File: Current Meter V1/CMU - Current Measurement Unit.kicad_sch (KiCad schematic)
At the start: 0 parts

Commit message: Initial commit
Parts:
- added C114, C115, C116, C117, C119, C122, C123, C124: 100nF, symbol Device:C
- added C118: 1uF, symbol Device:C
- added C120: 10uF, symbol Device:C
- added C121: 4.7uF, symbol Device:C
- added D101: PRTR5V0U2X, Package_TO_SOT_SMD:SOT-143, symbol Power_Protection:PRTR5V0U2X
- added J101: SWD Programming Header (ST-Link), symbol Connector_Generic:Conn_01x04
- added J102: I2C OLED Display Connector, symbol Connector_Generic:Conn_01x04
- added R104: 10K Ohms, symbol Device:R_US
- added R105, R108, R109, R110, R111, R112: 10k Ohms, symbol Device:R_US
- added R106: 3.3K Ohms, symbol Device:R_US
- added R107: 4.7K Ohms, symbol Device:R_US
- added R113, R114: 4.7k Ohms, symbol Device:R_US
- added TP101: SMD Test Point, TestPoint:TestPoint_Keystone_5019_Miniature, symbol bfr_utilities:SMD_Test_Point
- added U101: STM32L432KCUx, Package_DFN_QFN:QFN-32-1EP_5x5mm_P0.5mm_EP3.45x3.45mm, symbol MCU_ST_STM32L4:STM32L432KCUx
- added U104: A1308xLHxx-1, Package_TO_SOT_SMD:SOT-23W, symbol Sensor_Magnetic:A1308xLHxx-1
- added U105: MCP6002-xSN, symbol Amplifier_Operational:MCP6002-xSN
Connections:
- new net: C124.1, R110.1, R111.2, R112.1
- new net: R105.2, R110.2, U105.3 (+)
- new net: C122.1, D101.2 (I/O1), R106.2, R107.1, U101.6 (PA0)
- new net: C119.2, R104.1, U101.4 (NRST)
- new net: R108.1, U104.2 (V_{OUT})
- new net: R106.1, R109.2, U105.1
- new net: R108.2, R109.1, U105.2 (-)
- new net: C115.1, C118.1, U101.5 (VDDA)
- new net: C116.1, C117.1, U101.1 (VDD), U101.17 (VDD)
- new net: U105.6 (-), U105.7
- new net +3.3V: C121.1
- new net +3V3: D101.4 (VCC), J101.4 (Pin_4), J102.1 (Pin_1), R104.2, R111.1, R113.2, R114.2
- new net +5V: C114.1, C120.1, C123.1, U104.1 (V_{CC}), U105.8 (V+)
- new net GND: C114.2, C115.2, C116.2, C117.2, C118.2, C119.1, C120.2, C121.2, C122.2, C123.2, C124.2, D101.1 (GND), J101.3 (Pin_3), J102.2 (Pin_2), R105.1, R107.2, R112.2, U101.16 (VSS), U101.31 (PH3), U101.32 (VSS), U101.33 (VSS), U104.3 (GND), U105.4 (V-), U105.5 (+)
- new net SCL: J102.3 (Pin_3), R114.1, U101.29 (PB6)
- new net SDA: J102.4 (Pin_4), R113.1, U101.30 (PB7)
- new net SWCLK: J101.2 (Pin_2), U101.24 (PA14)
- new net SWDIO: J101.1 (Pin_1), U101.23 (PA13)
- no-connect marks 0 -> 1
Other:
- added sheet Old_Version (Old_Version.kicad_sch)

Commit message: test
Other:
- note added: "Test - Katie"
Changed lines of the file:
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@@
 	(generator_version "9.0")
 	(paper "A4")
+	(text "Test - Katie\n"
+		(exclude_from_sim no)
+		(at 214.376 36.576 0)
+		(effects
+			(font
+				(size 1.27 1.27)
+			)
+		)
+	)
 	(junction
 		(at 161.29 107.95)

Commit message: updated schematic
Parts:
- removed C119: 100nF, symbol Device:C
- removed R104: 10K Ohms, symbol Device:R_US
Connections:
- no-connect marks 1 -> 2
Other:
- note removed: "Test - Katie"
- moved on the sheet: C121

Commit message: Changes Added usb c power, 3v3 ldo, protection diode for hall output, capacitors and power rail on stm
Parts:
- removed J101: SWD Programming Header (ST-Link), symbol Connector_Generic:Conn_01x04
- added C1, C3: 10uF, symbol Device:C
- added C2: 22uF, symbol Device:C
- added C4: 100nF, symbol Device:C
- added D1: BAT54A, Package_TO_SOT_SMD:SOT-23, symbol Diode:BAT54A
- added J1: USB_C_Receptacle_PowerOnly_6P, symbol Connector:USB_C_Receptacle_PowerOnly_6P
- added R1, R2: 5.1k Ohms, symbol Device:R_US
- added U1: AMS1117-3.3, Package_TO_SOT_SMD:SOT-223-3_TabPin2, symbol Regulator_Linear:AMS1117-3.3
- R108: value 10k Ohms -> 4.7k Ohms
- R109: value 10k Ohms -> 20k Ohms
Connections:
- net +3V3: now also C115.1, C116.1, C117.1, C118.1, U101.1 (VDD), U101.17 (VDD), U101.5 (VDDA), C2.1, C3.1, C4.1, U1.2 (VO); no longer R111.1
- net +5V: now also R111.1, C1.1, D1.1, J1.A9 (VBUS), J1.B9 (VBUS), U1.3 (VI)
- net GND: now also C1.2, C2.2, C3.2, C4.2, J1.A12 (GND), J1.B12 (GND), J1.S1 (SHIELD), R1.2, R2.2, U1.1 (GND)
- net SCL: now also R113.1, U101.30 (PB7); no longer R114.1, U101.29 (PB6)
- net SDA: now also R114.1, U101.29 (PB6); no longer R113.1, U101.30 (PB7)
- net at R108.1, U104.2 (V_{OUT}): now also D1.3
- net at R106.1, R109.2, U105.1: now also TP101.1
- net SWCLK: no longer names the net of U101.24 (PA14)
- net SWDIO: no longer names the net of U101.23 (PA13)
- new net: J1.B5 (CC2), R2.1
- new net: J1.A5 (CC1), R1.1
- no-connect marks 2 -> 25
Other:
- moved on the sheet: C121, J102, R113, R114

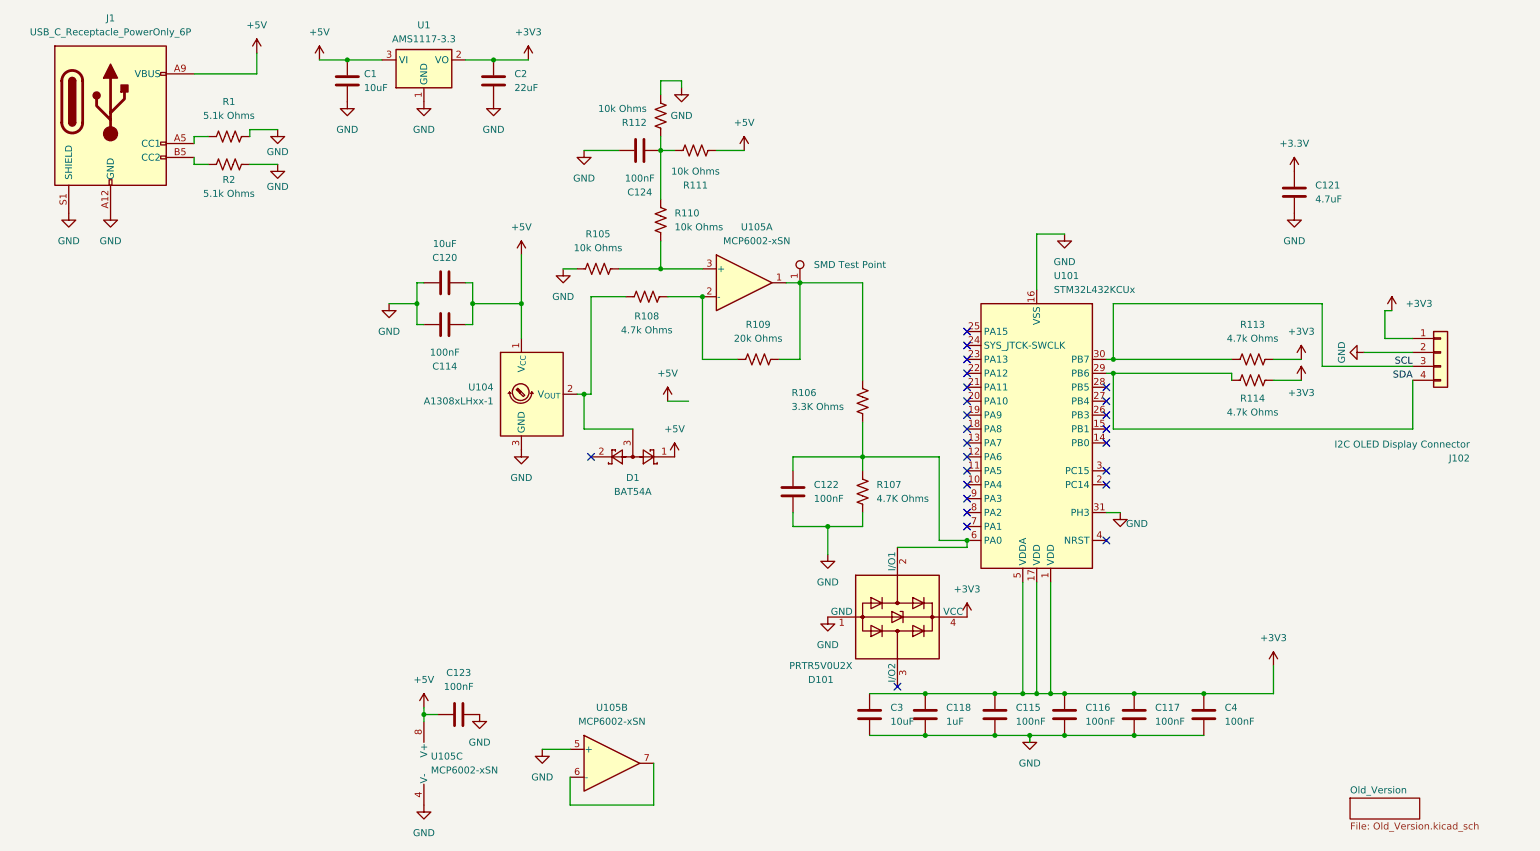
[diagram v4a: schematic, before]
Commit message: Redesign op amp circuit for 0-3.3v output previous design clipped to negative
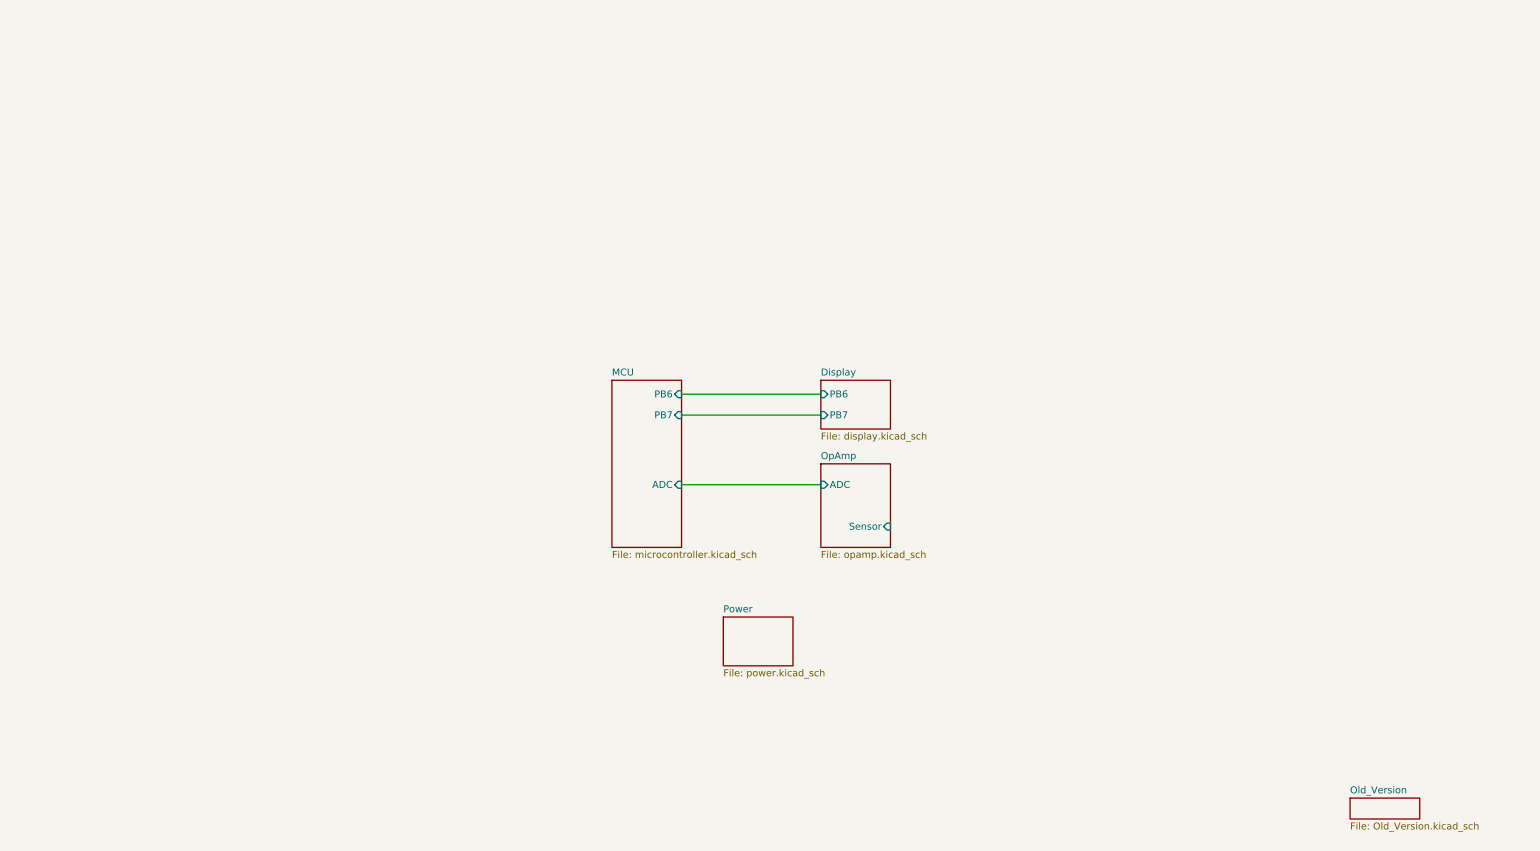
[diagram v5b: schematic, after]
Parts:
- removed C1, C120, C3: 10uF, symbol Device:C
- removed C114, C115, C116, C117, C122, C123, C124, C4: 100nF, symbol Device:C
- removed C118: 1uF, symbol Device:C
- removed C121: 4.7uF, symbol Device:C
- removed C2: 22uF, symbol Device:C
- removed D1: BAT54A, Package_TO_SOT_SMD:SOT-23, symbol Diode:BAT54A
- removed D101: PRTR5V0U2X, Package_TO_SOT_SMD:SOT-143, symbol Power_Protection:PRTR5V0U2X
- removed J1: USB_C_Receptacle_PowerOnly_6P, symbol Connector:USB_C_Receptacle_PowerOnly_6P
- removed J102: I2C OLED Display Connector, symbol Connector_Generic:Conn_01x04
- removed R1, R2: 5.1k Ohms, symbol Device:R_US
- removed R105, R110, R111, R112: 10k Ohms, symbol Device:R_US
- removed R106: 3.3K Ohms, symbol Device:R_US
- removed R107: 4.7K Ohms, symbol Device:R_US
- removed R108, R113, R114: 4.7k Ohms, symbol Device:R_US
- removed R109: 20k Ohms, symbol Device:R_US
- removed TP101: SMD Test Point, TestPoint:TestPoint_Keystone_5019_Miniature, symbol bfr_utilities:SMD_Test_Point
- removed U1: AMS1117-3.3, Package_TO_SOT_SMD:SOT-223-3_TabPin2, symbol Regulator_Linear:AMS1117-3.3
- removed U101: STM32L432KCUx, Package_DFN_QFN:QFN-32-1EP_5x5mm_P0.5mm_EP3.45x3.45mm, symbol MCU_ST_STM32L4:STM32L432KCUx
- removed U104: A1308xLHxx-1, Package_TO_SOT_SMD:SOT-23W, symbol Sensor_Magnetic:A1308xLHxx-1
- removed U105: MCP6002-xSN, symbol Amplifier_Operational:MCP6002-xSN
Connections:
- no-connect marks 25 -> 0
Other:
- added sheet Display (display.kicad_sch)
- added sheet MCU (microcontroller.kicad_sch)
- added sheet OpAmp (opamp.kicad_sch)
- added sheet Power (power.kicad_sch)
